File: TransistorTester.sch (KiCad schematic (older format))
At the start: 23 parts, among them IC1 ATMEGA8-P, IC2 78L05, J1 TEST POINTS, J2 POWER

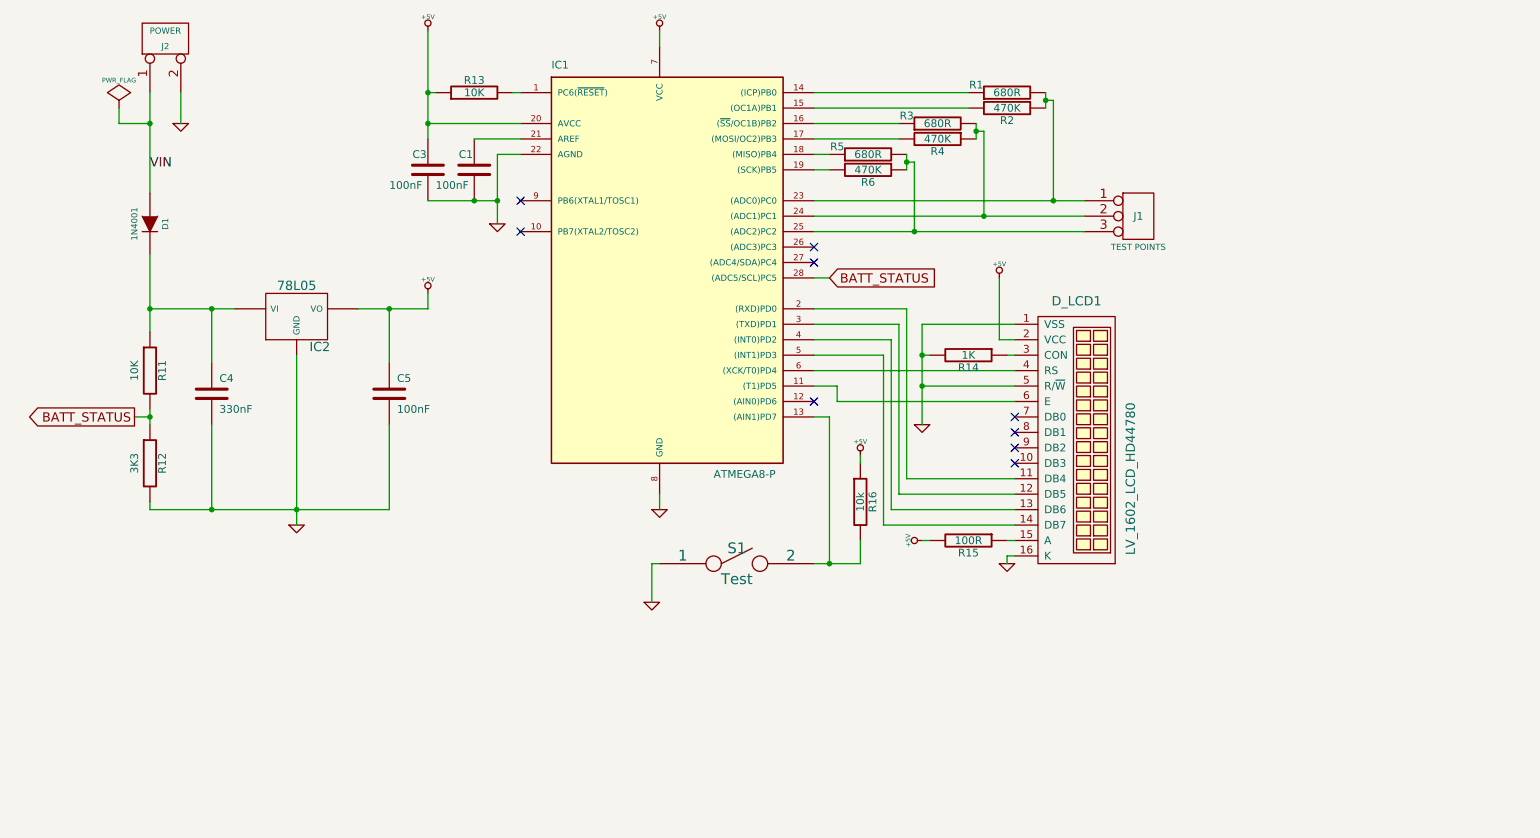
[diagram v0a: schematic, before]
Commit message: v.0.7: Added net names, pin-1 markers. Button moved to PCB edge
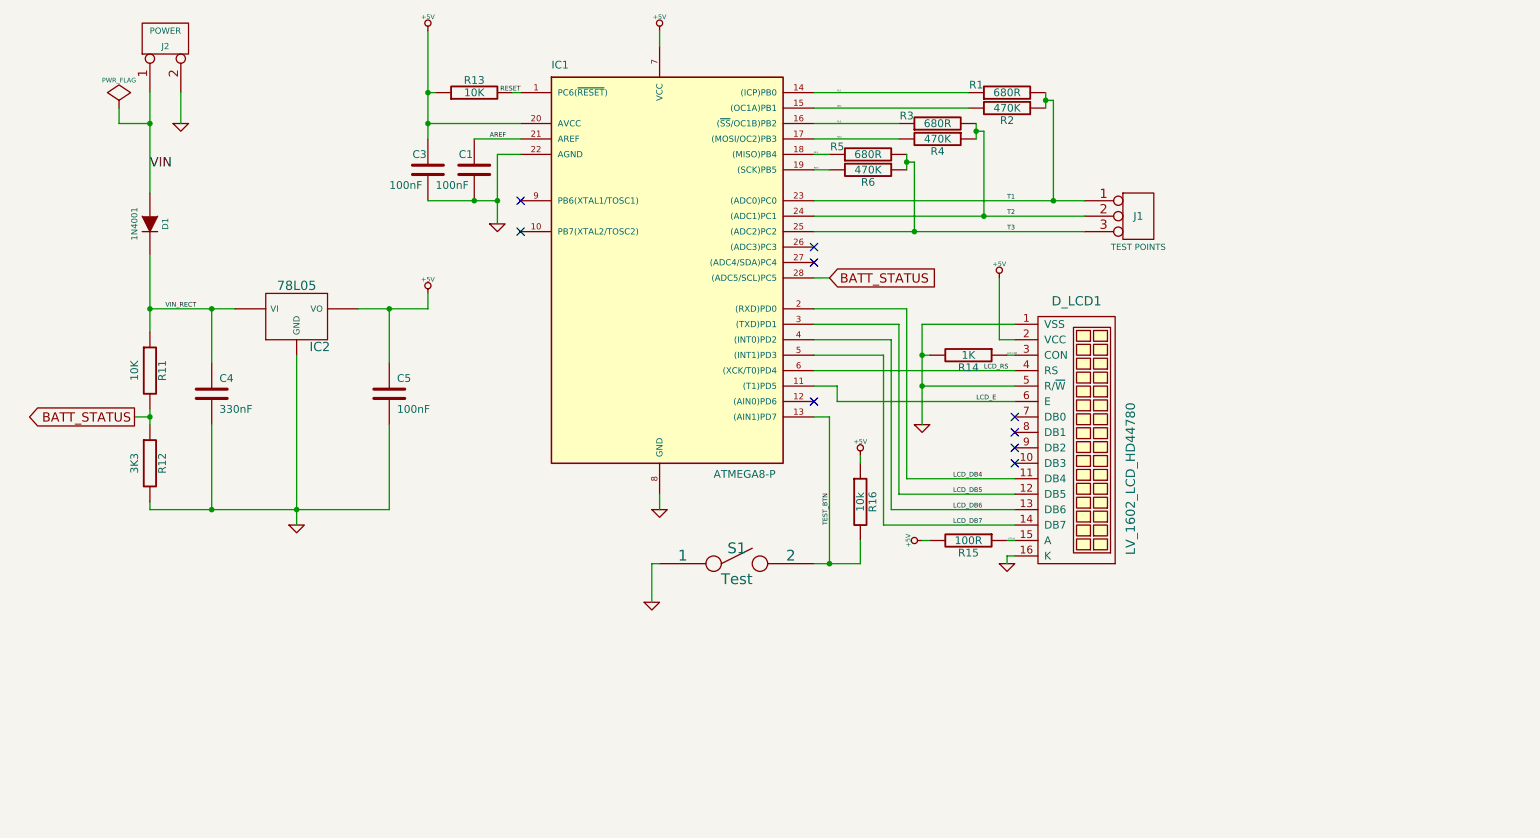
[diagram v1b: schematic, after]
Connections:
- net RESET: now reaches IC1.1 (PC6(~RESET~)), R13.2
- net LCD_E: now reaches D_LCD1.6 (E), IC1.11 ((T1)PD5)
- net TEST_BTN: now reaches IC1.13 ((AIN1)PD7), R16.2, S1.2
- net RL1: now reaches IC1.14 ((ICP)PB0), R1.1
- net RH1: now reaches IC1.15 ((OC1A)PB1), R2.2
- net RL2: now reaches IC1.16 ((~SS~/OC1B)PB2), R3.1
- net RH2: now reaches IC1.17 ((MOSI/OC2)PB3), R4.2
- net RL3: now reaches IC1.18 ((MISO)PB4), R5.1
- net RH3: now reaches IC1.19 ((SCK)PB5), R6.2
- net LCD_DB4: now reaches D_LCD1.11 (DB4), IC1.2 ((RXD)PD0)
- net AREF: now reaches C1.1, IC1.21 (AREF)
- net T1: now reaches IC1.23 ((ADC0)PC0), J1.1 (P1), R1.2, R2.1
- net T2: now reaches IC1.24 ((ADC1)PC1), J1.2 (PM), R3.2, R4.1
- net T3: now reaches IC1.25 ((ADC2)PC2), J1.3 (P3), R5.2, R6.1
- net LCD_DB5: now reaches D_LCD1.12 (DB5), IC1.3 ((TXD)PD1)
- net LCD_DB6: now reaches D_LCD1.13 (DB6), IC1.4 ((INT0)PD2)
- net LCD_DB7: now reaches D_LCD1.14 (DB7), IC1.5 ((INT1)PD3)
- net LCD_RS: now reaches D_LCD1.4 (RS), IC1.6 ((XCK/T0)PD4)
- net LCD_CON: now reaches D_LCD1.3 (CON), R14.1
- net VIN_RECT: now reaches C4.1, D1.2 (K), IC2.VI, R11.1
- net LCD_A: now reaches D_LCD1.15 (A), R15.1
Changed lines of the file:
@@
 Title "AVR Transistor Tester"
 Date "9 jul 2012"
-Rev "0.6"
+Rev "0.7"
 Comp "Released under the Creative Commons Attribution Share-Alike 3.0"
 Comment1 "http://lowvoltage.wordpress.com"
@@
 	6050 5150 6050 5000
 Connection ~ 5850 5150
+Text Label 5850 4900 1    30   ~ 0
+TEST_BTN
+Text Label 6650 4900 0    30   ~ 0
+LCD_DB7
+Text Label 6650 4800 0    30   ~ 0
+LCD_DB6
+Text Label 6650 4700 0    30   ~ 0
+LCD_DB5
+Text Label 6650 4600 0    30   ~ 0
+LCD_DB4
+Text Label 6800 4100 0    30   ~ 0
+LCD_E
+Text Label 6850 3900 0    30   ~ 0
+LCD_RS
+Text Label 7000 3800 0    10   ~ 0
+LCD_CON
+Text Label 3850 2100 2    30   ~ 0
+RESET
+Text Label 3650 2400 0    30   ~ 0
+AREF
+Text Label 1550 3500 0    30   ~ 0
+VIN_RECT
+Text Label 7000 2800 0    30   ~ 0
+T1
+Text Label 7000 2900 0    30   ~ 0
+T2
+Text Label 7000 3000 0    30   ~ 0
+T3
+Text Label 7050 5000 2    10   ~ 0
+LCD_A
+Text Label 5900 2100 0    10   ~ 0
+RL1
+Text Label 5900 2200 0    10   ~ 0
+RH1
+Text Label 5900 2300 0    10   ~ 0
+RL2
+Text Label 5900 2400 0    10   ~ 0
+RH2
+Text Label 5750 2500 0    10   ~ 0
+RL3
+Text Label 5750 2600 0    10   ~ 0
+RH3
 $EndSCHEMATC

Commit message: Added BOM files. Schematics cleanup
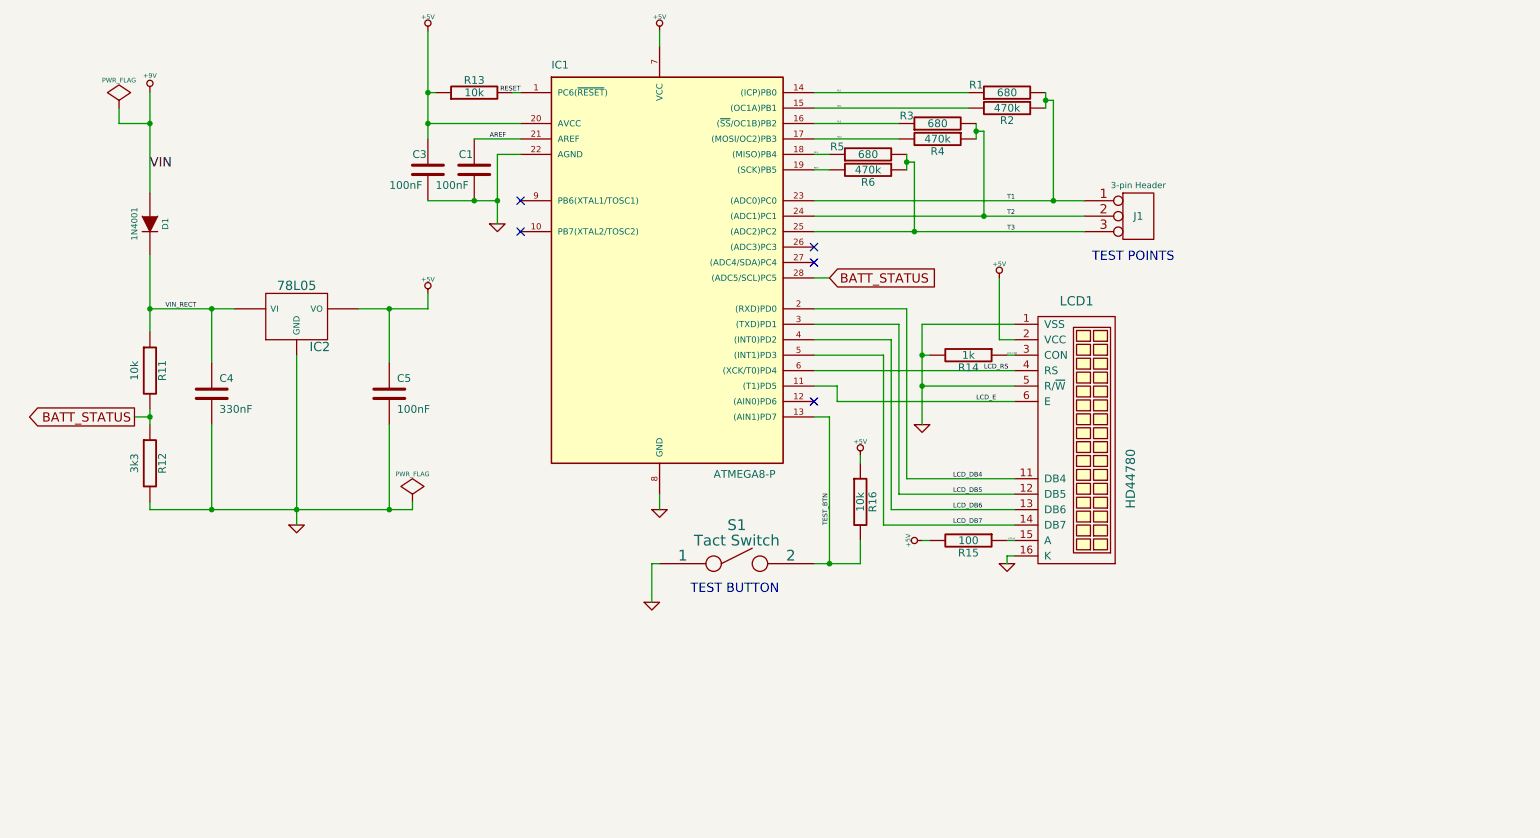
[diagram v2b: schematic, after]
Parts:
- removed D_LCD1: LV_1602_LCD_HD44780, symbol LV_1602_LCD_HD44780
- removed J2: POWER, symbol CONN_2
- added LCD1: HD44780, symbol LV_1602_LCD_HD44780_6+6
- J1: value TEST POINTS -> 3-pin Header
- R1, R3, R5: value 680R -> 680
- R11, R13: value 10K -> 10k
- R12: value 3K3 -> 3k3
- R14: value 1K -> 1k
- R15: value 100R -> 100
- R2, R4, R6: value 470K -> 470k
- S1: value Test -> Tact Switch
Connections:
- net +5V: now also LCD1.2 (VCC)
- net GND: now also LCD1.1 (VSS), LCD1.16 (K), LCD1.5 (R/~W)
- net LCD_A: now also LCD1.15 (A)
- net LCD_CON: now also LCD1.3 (CON)
- net LCD_DB4: now also LCD1.11 (DB4)
- net LCD_DB5: now also LCD1.12 (DB5)
- net LCD_DB6: now also LCD1.13 (DB6)
- net LCD_DB7: now also LCD1.14 (DB7)
- net LCD_E: now also LCD1.6 (E)
- net LCD_RS: now also LCD1.4 (RS)
- net VIN renamed +9V
- no-connect marks 9 -> 5
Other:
- note added: "TEST BUTTON"
- note added: "TEST POINTS"
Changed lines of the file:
@@
 Sheet 1 1
 Title "AVR Transistor Tester"
-Date "9 jul 2012"
-Rev "0.7"
+Date "21 jul 2012"
+Rev "0.8"
 Comp "Released under the Creative Commons Attribution Share-Alike 3.0"
 Comment1 "http://lowvoltage.wordpress.com"
@@
 Wire Wire Line
 	1450 3150 1450 3650
-Wire Wire Line
-	1650 2300 1650 2100
 Connection ~ 1450 4200
 Wire Wire Line
@@
 	1450 4750 1450 4800
 Wire Wire Line
-	1450 4800 3000 4800
+	1450 4800 3150 4800
 Connection ~ 2400 4800
 Connection ~ 1450 3500
 Wire Wire Line
 	5750 3300 5850 3300
-$Comp
-L GND #PWR01
-U 1 1 4F3FC649
-P 1650 2300
-F 0 "#PWR01" H 1650 2300 30  0001 C CNN
-F 1 "GND" H 1650 2230 30  0001 C CNN
-	1    1650 2300
-	1    0    0    -1
-$EndComp
-$Comp
-L CONN_2 J2
-U 1 1 4F3FC610
-P 1550 1750
-F 0 "J2" V 1500 1750 40  0000 C CNN
-F 1 "POWER" V 1600 1750 40  0000 C CNN
-	1    1550 1750
-	0    -1   -1   0
-$EndComp
 Text GLabel 5850 3300 2    60   Input ~ 0
 BATT_STATUS
@@
 AR Path="/4F3C1083" Ref="R12"  Part="1"
 F 0 "R12" V 1530 4500 50  0000 C CNN
-F 1 "3K3" V 1350 4500 50  0000 C CNN
+F 1 "3k3" V 1350 4500 50  0000 C CNN
 	1    1450 4500
 	1    0    0    -1
@@
 P 1450 3900
 F 0 "R11" V 1530 3900 50  0000 C CNN
-F 1 "10K" V 1350 3900 50  0000 C CNN
+F 1 "10k" V 1350 3900 50  0000 C CNN
 	1    1450 3900
 	1    0    0    -1
 $EndComp
 $Comp
-L PWR_FLAG #FLG02
+L PWR_FLAG #FLG01
 U 1 1 4F3C0DEB
 P 1250 2200
-F 0 "#FLG02" H 1250 2295 30  0001 C CNN
+F 0 "#FLG01" H 1250 2295 30  0001 C CNN
 F 1 "PWR_FLAG" H 1250 2380 30  0000 C CNN
 	1    1250 2200
 	1    0    0    -1
 $EndComp
-NoConn ~ 7050 4500
-NoConn ~ 7050 4400
-NoConn ~ 7050 4300
-NoConn ~ 7050 4200
 NoConn ~ 5750 4100
 NoConn ~ 5750 3200
@@
 NoConn ~ 3850 2800
 $Comp
-L GND #PWR03
+L GND #PWR02
 U 1 1 4F3C0B02
 P 2400 4900
-F 0 "#PWR03" H 2400 4900 30  0001 C CNN
+F 0 "#PWR02" H 2400 4900 30  0001 C CNN
 F 1 "GND" H 2400 4830 30  0001 C CNN
 	1    2400 4900
@@
 $EndComp
 $Comp
-L +5V #PWR04
+L +5V #PWR03
 U 1 1 4F3C0AFC
 P 3250 3400
-F 0 "#PWR04" H 3250 3490 20  0001 C CNN
+F 0 "#PWR03" H 3250 3490 20  0001 C CNN
 F 1 "+5V" H 3250 3490 30  0000 C CNN
 	1    3250 3400
@@
 $EndComp
 $Comp
-L GND #PWR05
+L GND #PWR04
 U 1 1 4F3C0A04
 P 4700 5400
-F 0 "#PWR05" H 4700 5400 30  0001 C CNN
+F 0 "#PWR04" H 4700 5400 30  0001 C CNN
 F 1 "GND" H 4700 5330 30  0001 C CNN
 	1    4700 5400
@@
 U 1 1 4F3C09DA
 P 5250 5150
-F 0 "S1" H 5250 5250 70  0000 C CNN
-F 1 "Test" H 5250 5050 70  0000 C CNN
+F 0 "S1" H 5250 5400 70  0000 C CNN
+F 1 "Tact Switch" H 5250 5300 70  0000 C CNN
 	1    5250 5150
 	1    0    0    -1
@@
 $EndComp
 $Comp
-L GND #PWR06
+L GND #PWR05
 U 1 1 4F3C0905
 P 4750 4800
-F 0 "#PWR06" H 4750 4800 30  0001 C CNN
+F 0 "#PWR05" H 4750 4800 30  0001 C CNN
 F 1 "GND" H 4750 4730 30  0001 C CNN
 	1    4750 4800
@@
 $EndComp
 $Comp
-L GND #PWR07
+L GND #PWR06
 U 1 1 4F3C07B5
 P 3700 2950
-F 0 "#PWR07" H 3700 2950 30  0001 C CNN
+F 0 "#PWR06" H 3700 2950 30  0001 C CNN
 F 1 "GND" H 3700 2880 30  0001 C CNN
 	1    3700 2950
@@
 $EndComp
 $Comp
-L +5V #PWR08
+L +5V #PWR07
 U 1 1 4F3C06A4
 P 4750 1700
-F 0 "#PWR08" H 4750 1790 20  0001 C CNN
+F 0 "#PWR07" H 4750 1790 20  0001 C CNN
 F 1 "+5V" H 4750 1790 30  0000 C CNN
 	1    4750 1700
@@
 $EndComp
 $Comp
-L +5V #PWR09
+L +5V #PWR08
 U 1 1 4F3C069B
 P 3250 1700
-F 0 "#PWR09" H 3250 1790 20  0001 C CNN
+F 0 "#PWR08" H 3250 1790 20  0001 C CNN
 F 1 "+5V" H 3250 1790 30  0000 C CNN
 	1    3250 1700
@@
 P 3550 2100
 F 0 "R13" V 3630 2100 50  0000 C CNN
-F 1 "10K" V 3550 2100 50  0000 C CNN
+F 1 "10k" V 3550 2100 50  0000 C CNN
 	1    3550 2100
 	0    -1   -1   0
@@
 P 6750 3800
 F 0 "R14" V 6830 3800 50  0000 C CNN
-F 1 "1K" V 6750 3800 50  0000 C CNN
+F 1 "1k" V 6750 3800 50  0000 C CNN
 	1    6750 3800
 	0    1    1    0
 $EndComp
 $Comp
-L GND #PWR010
+L GND #PWR09
 U 1 1 4F3BE686
 P 6450 4250
-F 0 "#PWR010" H 6450 4250 30  0001 C CNN
+F 0 "#PWR09" H 6450 4250 30  0001 C CNN
 F 1 "GND" H 6450 4180 30  0001 C CNN
 	1    6450 4250
@@
 $EndComp
 $Comp
-L +5V #PWR011
+L +5V #PWR010
 U 1 1 4F3BE586
 P 6950 3300
-F 0 "#PWR011" H 6950 3390 20  0001 C CNN
+F 0 "#PWR010" H 6950 3390 20  0001 C CNN
 F 1 "+5V" H 6950 3390 30  0000 C CNN
 	1    6950 3300
@@
 $EndComp
 $Comp
-L LV_1602_LCD_HD44780 D_LCD1
-U 1 1 4F53BDBA
+L LV_1602_LCD_HD44780_6+6 LCD1
+U 1 1 500B191B
 P 7400 4350
-F 0 "D_LCD1" V 8300 4400 60  0000 C CNN
-F 1 "LV_1602_LCD_HD44780" H 7150 4750 60  0000 C CNN
+F 0 "LCD1" V 8300 4400 60  0000 C CNN
+F 1 "HD44780" H 7150 4750 60  0000 C CNN
 	1    7400 4350
 	0    1    -1   0
@@
 P 7850 2900
 F 0 "J1" H 7850 2900 50  0000 C CNN
-F 1 "TEST POINTS" H 7850 2700 40  0000 C CNN
+F 1 "3-pin Header" H 7850 3100 40  0000 C CNN
 	1    7850 2900
 	1    0    0    -1
@@
 P 7000 2100
 F 0 "R1" V 7050 2300 50  0000 C CNN
-F 1 "680R" V 7000 2100 50  0000 C CNN
+F 1 "680" V 7000 2100 50  0000 C CNN
 	1    7000 2100
 	0    -1   -1   0
@@
 P 7000 2200
 F 0 "R2" V 7080 2200 50  0000 C CNN
-F 1 "470K" V 7000 2200 50  0000 C CNN
+F 1 "470k" V 7000 2200 50  0000 C CNN
 	1    7000 2200
 	0    1    1    0
@@
 P 6550 2400
 F 0 "R4" V 6630 2400 50  0000 C CNN
-F 1 "470K" V 6550 2400 50  0000 C CNN
+F 1 "470k" V 6550 2400 50  0000 C CNN
 	1    6550 2400
 	0    1    1    0
@@
 P 6550 2300
 F 0 "R3" V 6600 2500 50  0000 C CNN
-F 1 "680R" V 6550 2300 50  0000 C CNN
+F 1 "680" V 6550 2300 50  0000 C CNN
 	1    6550 2300
 	0    -1   -1   0
@@
 P 6100 2500
 F 0 "R5" V 6150 2700 50  0000 C CNN
-F 1 "680R" V 6100 2500 50  0000 C CNN
+F 1 "680" V 6100 2500 50  0000 C CNN
 	1    6100 2500
 	0    -1   -1   0
@@
 P 6100 2600
 F 0 "R6" V 6180 2600 50  0000 C CNN
-F 1 "470K" V 6100 2600 50  0000 C CNN
+F 1 "470k" V 6100 2600 50  0000 C CNN
 	1    6100 2600
 	0    1    1    0
@@
 $EndComp
 $Comp
-L GND #PWR012
+L GND #PWR011
 U 1 1 4F41114D
 P 7000 5150
-F 0 "#PWR012" H 7000 5150 30  0001 C CNN
+F 0 "#PWR011" H 7000 5150 30  0001 C CNN
 F 1 "GND" H 7000 5080 30  0001 C CNN
 	1    7000 5150
@@
 $EndComp
 $Comp
-L +5V #PWR013
+L +5V #PWR012
 U 1 1 4F411164
 P 6450 5000
-F 0 "#PWR013" H 6450 5090 20  0001 C CNN
+F 0 "#PWR012" H 6450 5090 20  0001 C CNN
 F 1 "+5V" H 6450 5090 30  0000 C CNN
 	1    6450 5000
@@
 P 6750 5000
 F 0 "R15" V 6830 5000 50  0000 C CNN
-F 1 "100R" V 6750 5000 50  0000 C CNN
+F 1 "100" V 6750 5000 50  0000 C CNN
 F 2 "R5" H 6750 5000 60  0001 C CNN
 	1    6750 5000
@@
 $EndComp
 $Comp
-L +5V #PWR014
+L +5V #PWR013
 U 1 1 4FFB3063
 P 6050 4450
-F 0 "#PWR014" H 6050 4540 20  0001 C CNN
+F 0 "#PWR013" H 6050 4540 20  0001 C CNN
 F 1 "+5V" H 6050 4540 30  0000 C CNN
 	1    6050 4450
@@
 Text Label 5750 2600 0    10   ~ 0
 RH3
+$Comp
+L +9V #PWR014
+U 1 1 500B1F38
+P 1450 2100
+F 0 "#PWR014" H 1450 2070 20  0001 C CNN
+F 1 "+9V" H 1450 2210 30  0000 C CNN
+	1    1450 2100
+	1    0    0    -1
+$EndComp
+$Comp
+L PWR_FLAG #FLG015
+U 1 1 500B1FB0
+P 3150 4750
+F 0 "#FLG015" H 3150 4845 30  0001 C CNN
+F 1 "PWR_FLAG" H 3150 4930 30  0000 C CNN
+	1    3150 4750
+	1    0    0    -1
+$EndComp
+Wire Wire Line
+	3150 4800 3150 4750
+Connection ~ 3000 4800
+Text Notes 7550 3200 0    60   ~ 0
+TEST POINTS
+Text Notes 4950 5350 0    60   ~ 0
+TEST BUTTON
 $EndSCHEMATC

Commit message: v.B.0.1: Auto-sleep, control pins changed!
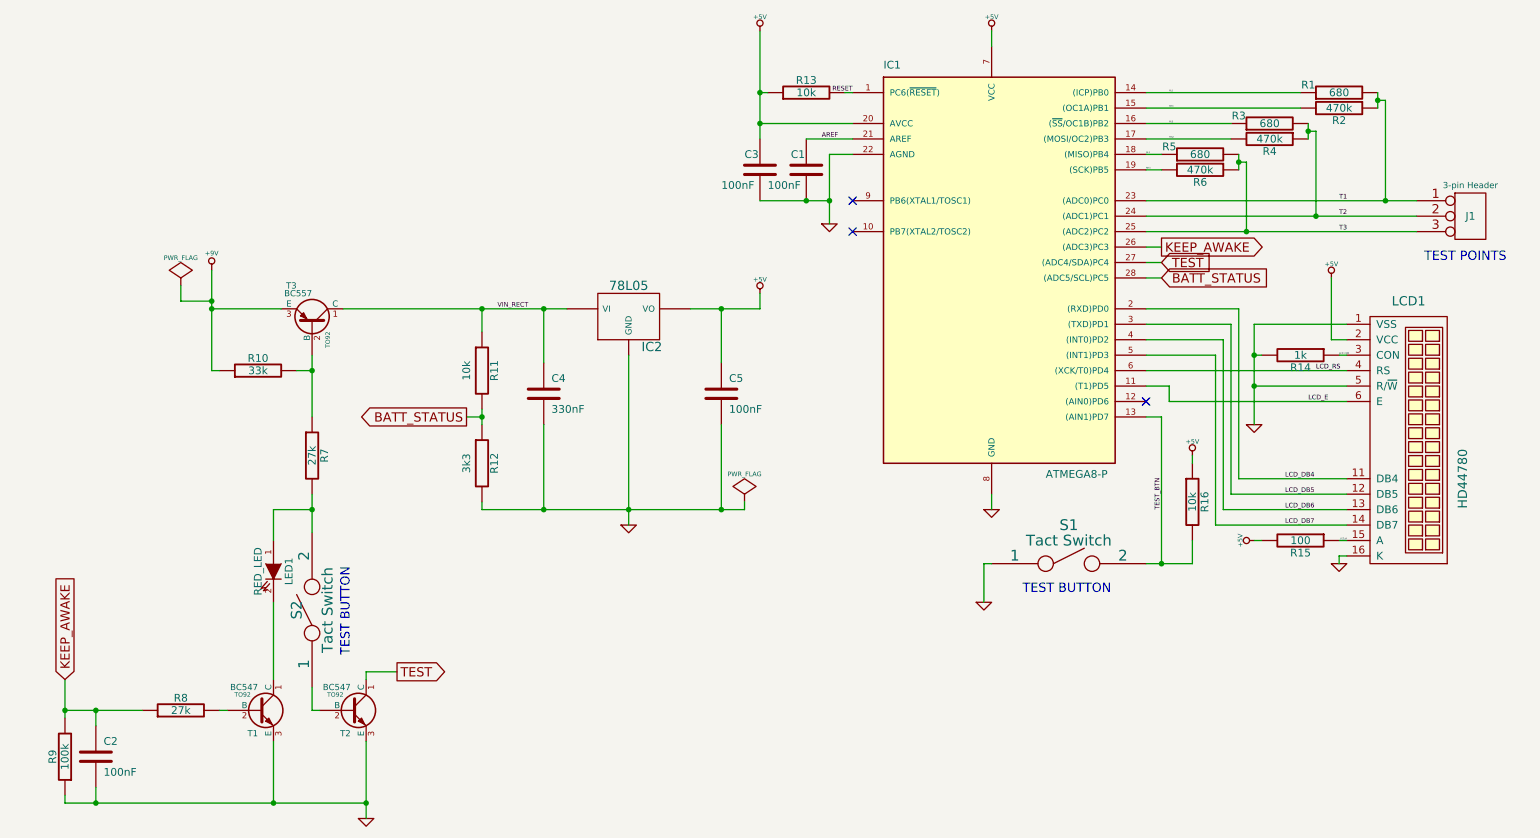
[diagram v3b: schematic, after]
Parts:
- removed D1: 1N4001, symbol DIODE
- added C2: 100nF, symbol C
- added LED1: RED_LED, symbol LED
- added R10: 33k, symbol R
- added R7, R8: 27k, symbol R
- added R9: 100k, symbol R
- added S2: Tact Switch, symbol SPST
- added T1, T2: BC547, TO92, symbol BC547
- added T3: BC557, TO92, symbol BC557
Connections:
- net +9V: now also R10.1, T3.3 (E)
- net GND: now also C2.2, R9.1, T1.3 (E), T2.3 (E)
- net VIN_RECT: now also T3.1 (C)
- net KEEP_AWAKE: now reaches IC1.26 ((ADC3)PC3)
- net KEEP_AWAKE: now also C2.1, R8.1, R9.2
- net TEST: now reaches IC1.27 ((ADC4/SDA)PC4)
- net TEST: now also T2.1 (C)
- new net: R10.2, R7.1, T3.2 (B)
- new net: LED1.1 (A), R7.2, S2.2
- new net: S2.1, T2.2 (B)
- new net: LED1.2 (K), T1.1 (C)
- new net: R8.2, T1.2 (B)
- no-connect marks 5 -> 3
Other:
- moved on the sheet: C1, C3, C4, C5, IC1, IC2, J1, LCD1, R1, R11, R12, R13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
